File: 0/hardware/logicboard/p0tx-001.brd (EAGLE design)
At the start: 91 x 57 mm, 29 parts, among them IC1 LTC485N, IC2 LTC485N, IC3 LTC485N, IC4 LTC485N, J0 DC5V, J10 DIN5, J7 DIN5, J8 DIN5, J9 DIN5, X9 NELTRON-7810-XPXC

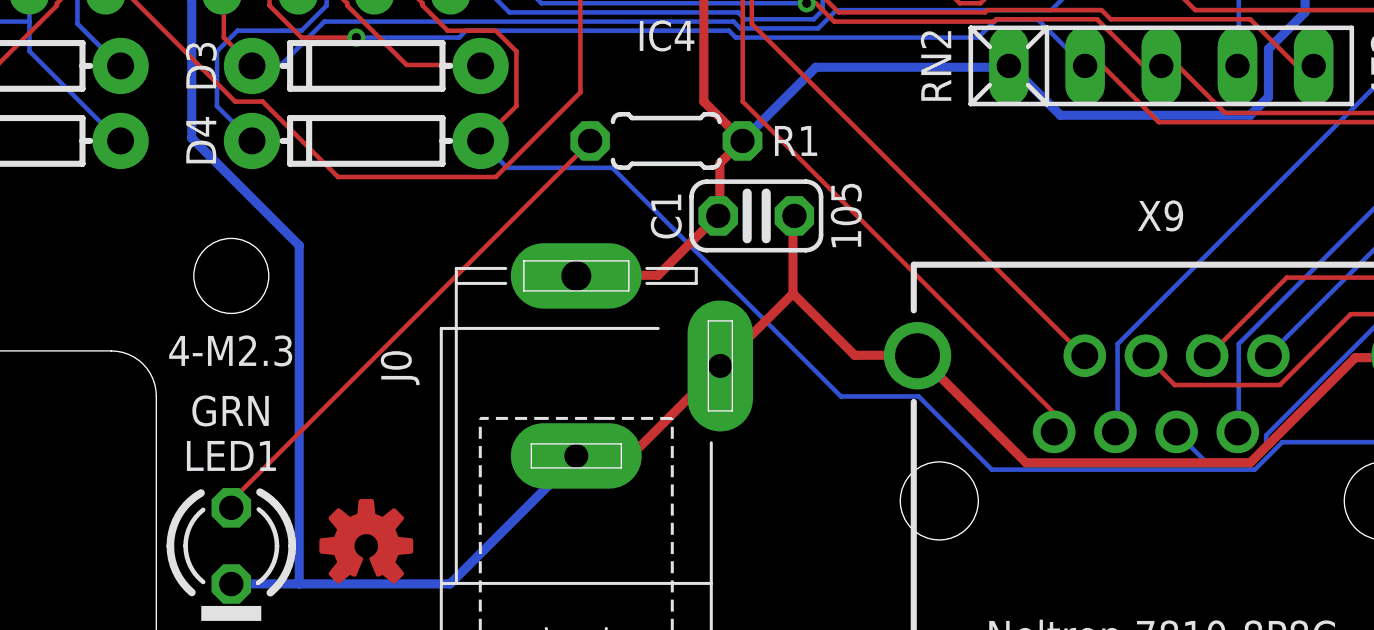
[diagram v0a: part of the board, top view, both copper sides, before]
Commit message: Replaced Rs with RN.
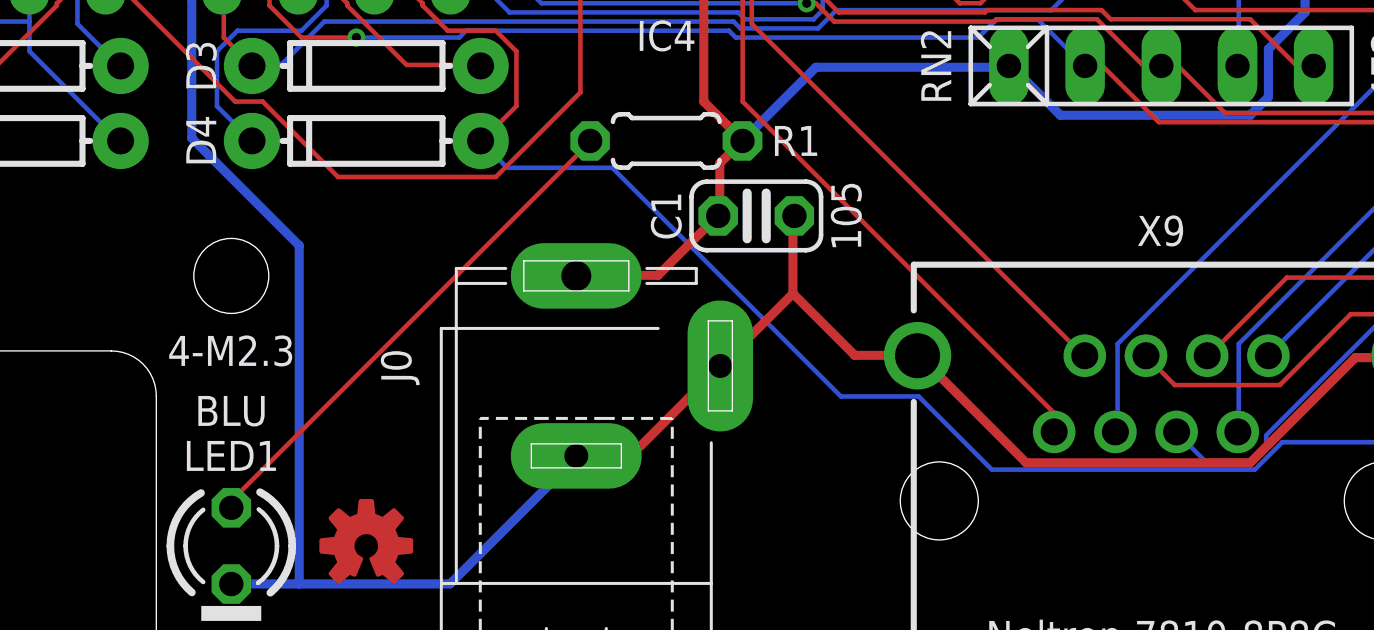
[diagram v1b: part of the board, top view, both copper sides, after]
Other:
- board text added: "BLU"
- board text removed: "GRN"
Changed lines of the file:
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@@
 <text x="45.5" y="2" size="1" layer="25" align="center">Neltron 7810-8P8C</text>
 <text x="6.5" y="38" size="1" layer="25" align="center">2-TLP2630</text>
-<text x="14.5" y="9.5" size="1" layer="25" align="center">GRN</text>
+<text x="14.5" y="9.5" size="1" layer="25" align="center">BLU</text>
 <text x="73" y="20.5" size="1" layer="25" align="center">4-LCT485</text>
 <text x="54.5" y="28.5" size="1" layer="25" rot="R90" align="center">221</text>
@@
 </element>
 <element name="X9" library="con-rj45" package="NELTRON-7810-XPXC-FOOTPRINT" value="NELTRON-7810-XPXC" x="45.5" y="6.5" smashed="yes" rot="R180">
-<attribute name="NAME" x="45.5" y="16" size="1" layer="25" rot="R180" align="center"/>
+<attribute name="NAME" x="45.5" y="15.5" size="1" layer="25" rot="R180" align="center"/>
 <attribute name="VALUE" x="45.5" y="5.5" size="1" layer="27" rot="R180" align="center"/>
 </element>

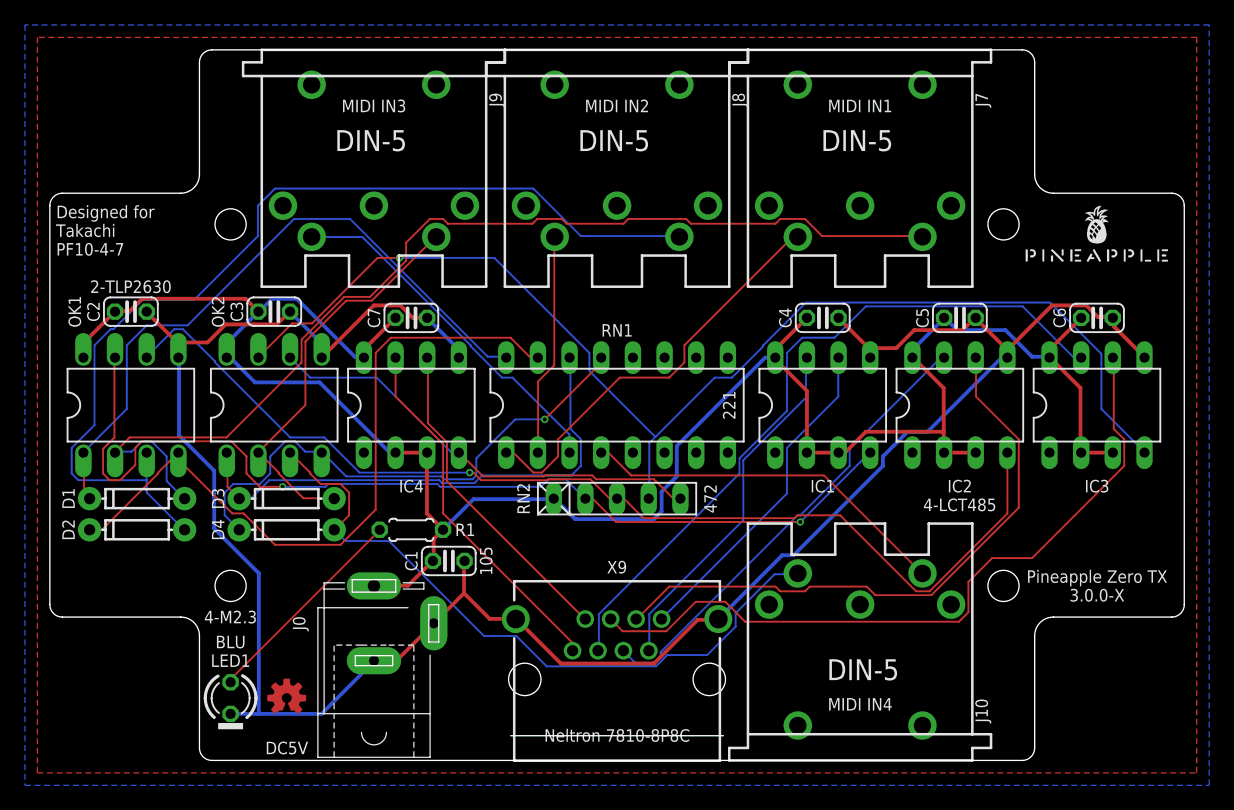
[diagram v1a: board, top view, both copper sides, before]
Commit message: Fixed wiring of 0.
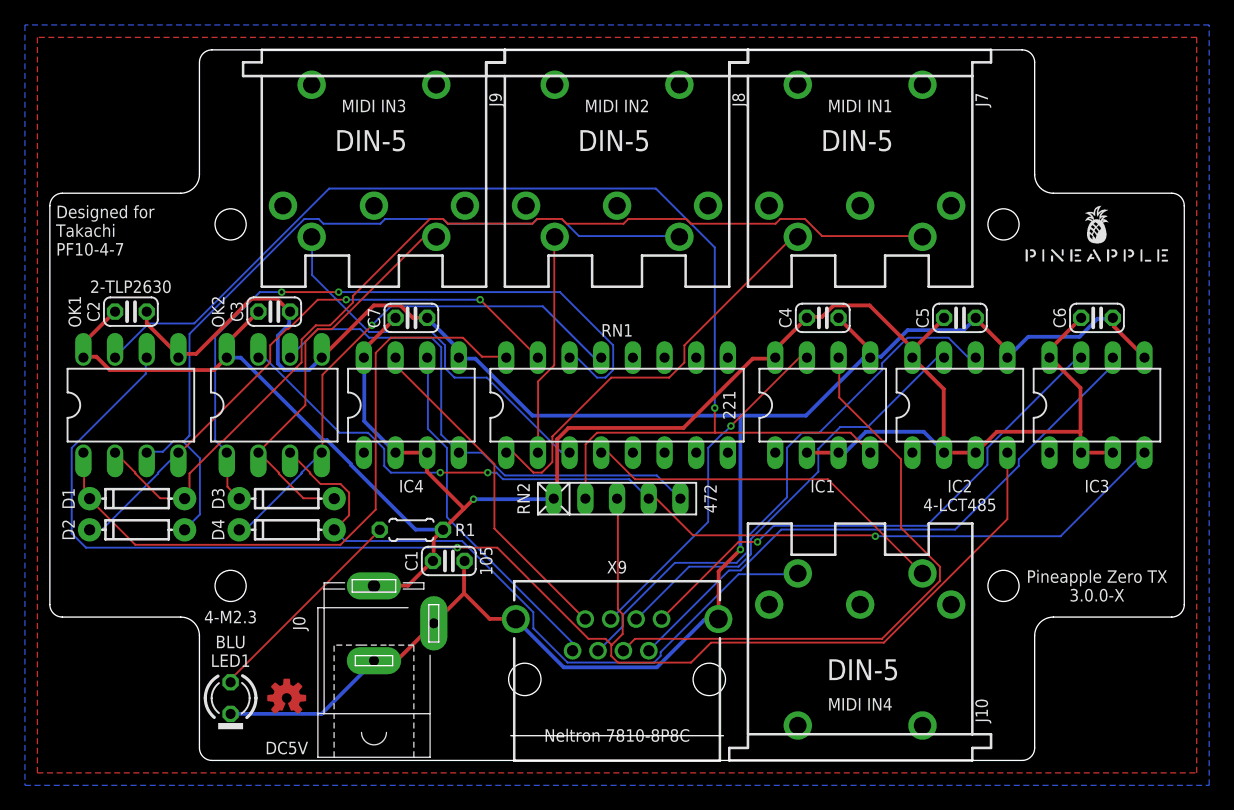
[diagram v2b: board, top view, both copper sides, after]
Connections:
- net TX1+: now also X9.4; no longer X9.1
- net TX1-: now also X9.5; no longer X9.2
- net TX2+: now also X9.6; no longer X9.3
- net TX2-: now also X9.3; no longer X9.4
- net TX3+: now also X9.2; no longer X9.5
- net TX3-: now also X9.1; no longer X9.6
- net TX4+: now also X9.8; no longer X9.7
- net TX4-: now also X9.7; no longer X9.8
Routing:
- net N$5: track 86.5 -> 118.9 mm
- net TX1+: track 26.9 -> 49.0 mm
- net TX: track 80.1 -> 98.8 mm, vias 2 -> 1
- net N$10: track 98.5 -> 80.6 mm, vias 1 -> 3
- net MI2RTN: track 79.9 -> 64.7 mm
- net TX3-: track 57.0 -> 43.2 mm, vias 0 -> 1
- net N$8: track 41.9 -> 55.4 mm, vias 0 -> 2
- net TX3+: track 59.0 -> 47.6 mm
- net N$7: track 57.1 -> 46.4 mm, vias 0 -> 2
- net GND: track 182.5 -> 175.8 mm, vias 0 -> 1
- net N$6: track 36.1 -> 42.0 mm
- net MI1RTN: track 85.1 -> 79.6 mm
- net VCC: track 172.7 -> 177.3 mm, vias 0 -> 1
- net TX2+: track 48.8 -> 45.2 mm
- net TX4-: track 29.4 -> 27.3 mm
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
